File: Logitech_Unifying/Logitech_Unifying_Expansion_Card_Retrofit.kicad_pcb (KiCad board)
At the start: 2 copper layers, 24 x 27.3 mm, 9 parts, among them P1 USB_C_Plug_USB2.0, U1 AP2112K-3.3

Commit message: v1
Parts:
- removed C1, C2: 10uF, Capacitor_SMD:C_0805_2012Metric
- removed U1: AP2112K-3.3, Package_TO_SOT_SMD:SOT-23-5
- added DN: Castellated_2, Expansion_Card:Castellated_2, F.Cu at (138.9, 138.6)
- added DP: Castellated_2, Expansion_Card:Castellated_2, F.Cu at (141.1, 138.6)
- added GND: Logitech_Unifying_Reciever, Expansion_Card:Logitech_Unifying_Reciever_no_pads, F.Cu at (140.0, 152.0)
- added GND: Castellated_2, Expansion_Card:Castellated_2, F.Cu at (143.6, 138.6)
- added VBUS: Castellated_2, Expansion_Card:Castellated_2, F.Cu at (136.4, 138.6)
- moved R1 4.28 mm to (132.7, 132.3), turned to 90 degrees
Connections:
- P1 pad A6: (no net) -> /USB_DP
- P1 pad A7: (no net) -> /USB_DN
- P1 pad B5: (no net) -> unconnected-(P1-VCONN-PadB5)
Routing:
- net VBUS: track 0.00 -> 20.0 mm, vias 0 -> 2
- net /USB_DP: track 0.00 -> 9.74 mm, vias 0 -> 2
- net /USB_DN: track 0.00 -> 9.55 mm
- net Net-(P1-CC): track 0.00 -> 9.55 mm, vias 0 -> 2
- net GND: track 0.00 -> 6.21 mm, vias 8 -> 9
- added copper zone on B.Cu, net GND
- added copper zone on F.Cu, net GND
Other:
- outline, holes or cut-outs redrawn
- board text added: "5.1k"

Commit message: small revision for cadlab test
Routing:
- net GND: track 6.21 -> 5.86 mm, vias 9 -> 19
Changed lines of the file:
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@@
     (pad_to_mask_clearance 0)
     (pcbplotparams
-      (layerselection 0x0001000_7ffffffe)
+      (layerselection 0x00010fc_ffffffff)
       (plot_on_all_layers_selection 0x0000000_00000000)
       (disableapertmacros false)
@@
       (usegerberattributes true)
       (usegerberadvancedattributes true)
-      (creategerberjobfile true)
+      (creategerberjobfile false)
       (dashed_line_dash_ratio 12.000000)
       (dashed_line_gap_ratio 3.000000)
@@
       (sketchpadsonfab false)
       (subtractmaskfromsilk false)
-      (outputformat 3)
+      (outputformat 1)
       (mirror false)
       (drillshape 0)
       (scaleselection 1)
-      (outputdirectory "")
+      (outputdirectory "assembly/")
     )
   )
@@
     (property "ki_keywords" "r resistor")
     (attr smd)
-    (fp_text reference "R1" (at 0 -1.43) (layer "F.SilkS")
-        (effects (font (size 0.5842 0.5842) (thickness 0.1016)))
+    (fp_text reference "R1" (at 0.1 -1.55) (layer "F.SilkS")
+        (effects (font (size 0.8 0.8) (thickness 0.1016)))
     )
     (fp_text value "5.1k" (at 0 1.43 90) (layer "F.Fab")
@@
     (attr smd)
     (fp_text reference "P1" (at 0 2.04) (layer "F.SilkS")
-        (effects (font (size 0.5842 0.5842) (thickness 0.1016)))
+        (effects (font (size 0.8 0.8) (thickness 0.1016)))
     )
     (fp_text value "USB_C_Plug_USB2.0" (at 0 -1.96) (layer "F.Fab")
@@
     (tags "Through hole pin header THT 1x01 2.54mm single row")
     (attr through_hole)
-    (fp_text reference "VBUS" (at 0 -2.33) (layer "F.SilkS")
+    (fp_text reference "VBUS" (at -1.3 -2.35) (layer "F.SilkS")
         (effects (font (size 1 1) (thickness 0.15)))
     )
@@
     (tags "Through hole pin header THT 1x01 2.54mm single row")
     (attr through_hole)
-    (fp_text reference "DN" (at 0 -2.33) (layer "F.SilkS")
+    (fp_text reference "DN" (at -0.2 -2.3) (layer "F.SilkS")
         (effects (font (size 1 1) (thickness 0.15)))
     )
@@
     (tags "Through hole pin header THT 1x01 2.54mm single row")
     (attr through_hole)
-    (fp_text reference "GND" (at 0 -2.33) (layer "F.SilkS")
+    (fp_text reference "GND" (at 0.45 -2.3) (layer "F.SilkS")
         (effects (font (size 1 1) (thickness 0.15)))
     )
@@
   (gr_circle (center 128.7 146.5) (end 131.15 146.5)
     (stroke (width 0.05) (type solid)) (fill none) (layer "F.CrtYd"))
-  (gr_text "5.1k" (at 130.85 133.15) (layer "F.SilkS")
-    (effects (font (size 0.5842 0.5842) (thickness 0.1016)))
+  (gr_text "5.1k" (at 130.6 133.35) (layer "F.SilkS")
+    (effects (font (size 0.8 0.8) (thickness 0.1016)))
   )
   (segment (start 137.232999 129.22) (end 136.562999 129.89) (width 0.1524) (layer "F.Cu") (net 1))
   (segment (start 142.75 131.05) (end 142.75 129.067001) (width 0.1524) (layer "F.Cu") (net 1))
+  (via (at 128.8 145) (size 0.5) (drill 0.3) (layers "F.Cu" "B.Cu") (net 1))
+  (via (at 128.85 148.05) (size 0.5) (drill 0.3) (layers "F.Cu" "B.Cu") (net 1))
   (via (at 133.985 127.8255) (size 0.5) (drill 0.3) (layers "F.Cu" "B.Cu") (net 1))
+  (via (at 151.25 148.05) (size 0.5) (drill 0.3) (layers "F.Cu" "B.Cu") (net 1))
+  (via (at 129.9 147.55) (size 0.5) (drill 0.3) (layers "F.Cu" "B.Cu") (net 1))
   (via (at 137.9 135) (size 0.5) (drill 0.3) (layers "F.Cu" "B.Cu") (net 1))
   (via (at 133.985 128.778) (size 0.5) (drill 0.3) (layers "F.Cu" "B.Cu") (net 1))
+  (via (at 130.3 146.5) (size 0.5) (drill 0.3) (layers "F.Cu" "B.Cu") (net 1))
+  (via (at 129.85 145.45) (size 0.5) (drill 0.3) (layers "F.Cu" "B.Cu") (net 1))
+  (via (at 151.3 145) (size 0.5) (drill 0.3) (layers "F.Cu" "B.Cu") (net 1))
+  (via (at 149.8 146.5) (size 0.5) (drill 0.3) (layers "F.Cu" "B.Cu") (net 1))
   (via (at 134.9375 127.8255) (size 0.5) (drill 0.3) (layers "F.Cu" "B.Cu") (net 1))
+  (via (at 150.25 145.45) (size 0.5) (drill 0.3) (layers "F.Cu" "B.Cu") (net 1))
   (via (at 145.0975 127.8255) (size 0.5) (drill 0.3) (layers "F.Cu" "B.Cu") (net 1))
+  (via (at 150.2 147.55) (size 0.5) (drill 0.3) (layers "F.Cu" "B.Cu") (net 1))
   (via (at 145.0975 128.778) (size 0.5) (drill 0.3) (layers "F.Cu" "B.Cu") (net 1))
   (via (at 134.9375 128.778) (size 0.5) (drill 0.3) (layers "F.Cu" "B.Cu") (net 1))
@@
   (via (at 145.9865 128.778) (size 0.5) (drill 0.3) (layers "F.Cu" "B.Cu") (net 1))
   (segment (start 143.42 129.88) (end 142.75 129.21) (width 0.1524) (layer "B.Cu") (net 1))
-  (segment (start 142.75 129.21) (end 142.75 128.8585) (width 0.1524) (layer "B.Cu") (net 1))
   (segment (start 137.25 130.991499) (end 137.25 129.0085) (width 0.1524) (layer "B.Cu") (net 1))
   (segment (start 136.25 131.8) (end 134.925 133.125) (width 0.1524) (layer "F.Cu") (net 2))
   (segment (start 139.259204 129.076205) (end 139.259204 131.190796) (width 0.1524) (layer "F.Cu") (net 2))
-  (segment (start 138.65 131.8) (end 138.7 131.75) (width 0.1524) (layer "F.Cu") (net 2))
   (segment (start 139.259204 131.190796) (end 138.65 131.8) (width 0.1524) (layer "F.Cu") (net 2))
   (segment (start 134.925 133.125) (end 132.7 133.125) (width 0.1524) (layer "F.Cu") (net 2))
@@
   (segment (start 139.732999 129.05) (end 139.732999 129.800001) (width 0.2) (layer "F.Cu") (net 4))
   (segment (start 139.757999 131.691501) (end 139.757999 129.825001) (width 0.2) (layer "F.Cu") (net 4))
-  (segment (start 141.1 138.026014) (end 141.001254 138.12476) (width 0.2) (layer "F.Cu") (net 4))
   (via (at 139.65 131.7995) (size 0.5) (drill 0.3) (layers "F.Cu" "B.Cu") (net 4))
   (via (at 141.1 134) (size 0.5) (drill 0.3) (layers "F.Cu" "B.Cu") (net 4))
@@
         (xy 152.3 154.9)
         (xy 127.05 154.95)
-        (xy 126.95 126.25)
-        (xy 126.95 126.25)
       )
     )

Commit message: small change to test cadlab
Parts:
- moved R1 1.16 mm to (133.8, 131.8), turned to 180 degrees
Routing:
- net Net-(P1-CC): track 9.47 -> 7.05 mm
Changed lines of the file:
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@@
   (net 6 "unconnected-(P1-VCONN-PadB5)")
   (footprint "Resistor_SMD:R_0603_1608Metric" (layer "F.Cu")
-    (at 132.7 132.3 90)
+    (at 133.75 131.8 180)
     (descr "Resistor SMD 0603 (1608 Metric), square (rectangular) end terminal, IPC_7351 nominal, (Body size source: IPC-SM-782 page 72, https://www.pcb-3d.com/wordpress/wp-content/uploads/ipc-sm-782a_amendment_1_and_2.pdf), generated with kicad-footprint-generator")
     (tags "resistor")
@@
     (property "ki_keywords" "r resistor")
     (attr smd)
-    (fp_text reference "R1" (at 0.1 -1.55) (layer "F.SilkS")
+    (fp_text reference "R1" (at 0.1 -1.55 90) (layer "F.SilkS")
         (effects (font (size 0.8 0.8) (thickness 0.1016)))
     )
-    (fp_text value "5.1k" (at 0 1.43 90) (layer "F.Fab")
+    (fp_text value "5.1k" (at 0 1.43) (layer "F.Fab")
         (effects (font (size 1 1) (thickness 0.15)))
     )
-    (fp_text user "${REFERENCE}" (at 0 0 90) (layer "F.Fab")
+    (fp_text user "${REFERENCE}" (at 0 0) (layer "F.Fab")
         (effects (font (size 1 1) (thickness 0.15)))
     )
@@
     (fp_line (start 0.8 0.4125) (end -0.8 0.4125)
       (stroke (width 0.1) (type solid)) (layer "F.Fab"))
-    (pad "1" smd roundrect (at -0.825 0 90) (size 0.8 0.95) (layers "F.Cu" "F.Paste" "F.Mask") (roundrect_rratio 0.25)
+    (pad "1" smd roundrect (at -0.825 0 180) (size 0.8 0.95) (layers "F.Cu" "F.Paste" "F.Mask") (roundrect_rratio 0.25)
       (net 2 "Net-(P1-CC)") (pintype "passive"))
-    (pad "2" smd roundrect (at 0.825 0 90) (size 0.8 0.95) (layers "F.Cu" "F.Paste" "F.Mask") (roundrect_rratio 0.25)
+    (pad "2" smd roundrect (at 0.825 0 180) (size 0.8 0.95) (layers "F.Cu" "F.Paste" "F.Mask") (roundrect_rratio 0.25)
       (net 1 "GND") (pintype "passive"))
     (model "${KICAD6_3DMODEL_DIR}/Resistor_SMD.3dshapes/R_0603_1608Metric.wrl"
@@
   (gr_circle (center 128.7 146.5) (end 131.15 146.5)
     (stroke (width 0.05) (type solid)) (fill none) (layer "F.CrtYd"))
-  (gr_text "5.1k" (at 130.6 133.35) (layer "F.SilkS")
+  (gr_text "5.1k" (at 132.5 134.05 90) (layer "F.SilkS")
     (effects (font (size 0.8 0.8) (thickness 0.1016)))
   )
@@
   (segment (start 143.42 129.88) (end 142.75 129.21) (width 0.1524) (layer "B.Cu") (net 1))
   (segment (start 137.25 130.991499) (end 137.25 129.0085) (width 0.1524) (layer "B.Cu") (net 1))
-  (segment (start 136.25 131.8) (end 134.925 133.125) (width 0.1524) (layer "F.Cu") (net 2))
+  (segment (start 136.25 131.8) (end 134.575 131.8) (width 0.1524) (layer "F.Cu") (net 2))
   (segment (start 139.259204 129.076205) (end 139.259204 131.190796) (width 0.1524) (layer "F.Cu") (net 2))
   (segment (start 139.259204 131.190796) (end 138.65 131.8) (width 0.1524) (layer "F.Cu") (net 2))
-  (segment (start 134.925 133.125) (end 132.7 133.125) (width 0.1524) (layer "F.Cu") (net 2))
   (via (at 138.65 131.8) (size 0.5) (drill 0.3) (layers "F.Cu" "B.Cu") (net 2))
   (via (at 136.25 131.8) (size 0.5) (drill 0.3) (layers "F.Cu" "B.Cu") (net 2))

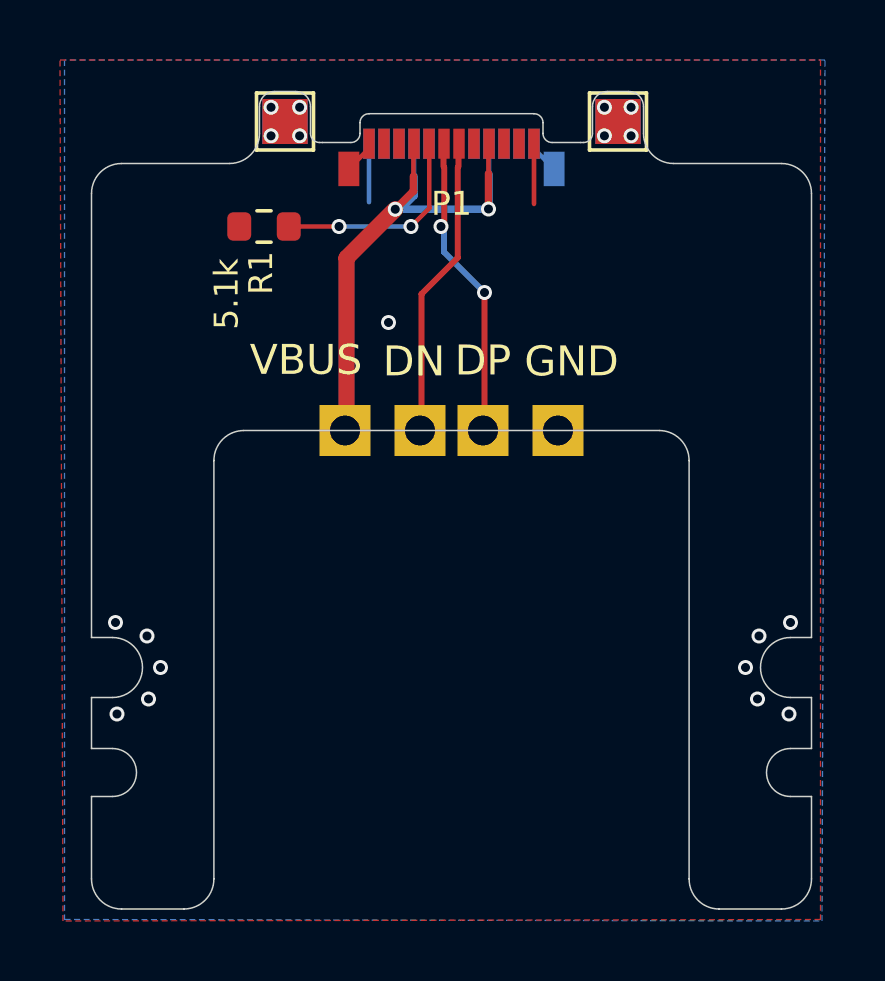
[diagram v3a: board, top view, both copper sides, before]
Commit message: flipped USB-C relative to reciever
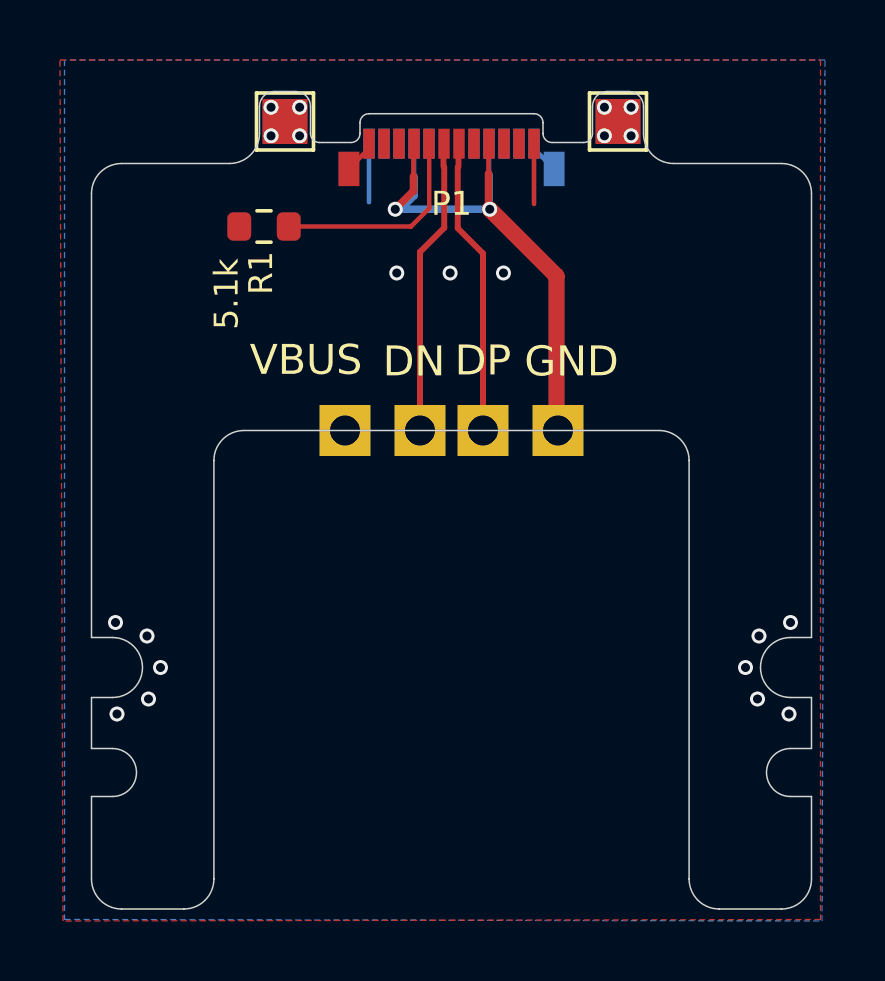
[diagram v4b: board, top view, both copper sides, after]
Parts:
- removed the GND at (140.0, 152.0)
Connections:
- DN pad 1: /USB_DN -> /USB_DP
- DP pad 1: /USB_DP -> /USB_DN
- GND pad 1: GND -> VBUS
- VBUS pad 1: VBUS -> GND
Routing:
- net VBUS: track 20.0 -> 20.8 mm
- net /USB_DP: track 9.60 -> 9.86 mm, vias 2 -> 0
- net Net-(P1-CC): vias 2 -> 0
- net GND: vias 19 -> 21

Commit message: increase USB-C mask bridge width for manufacture
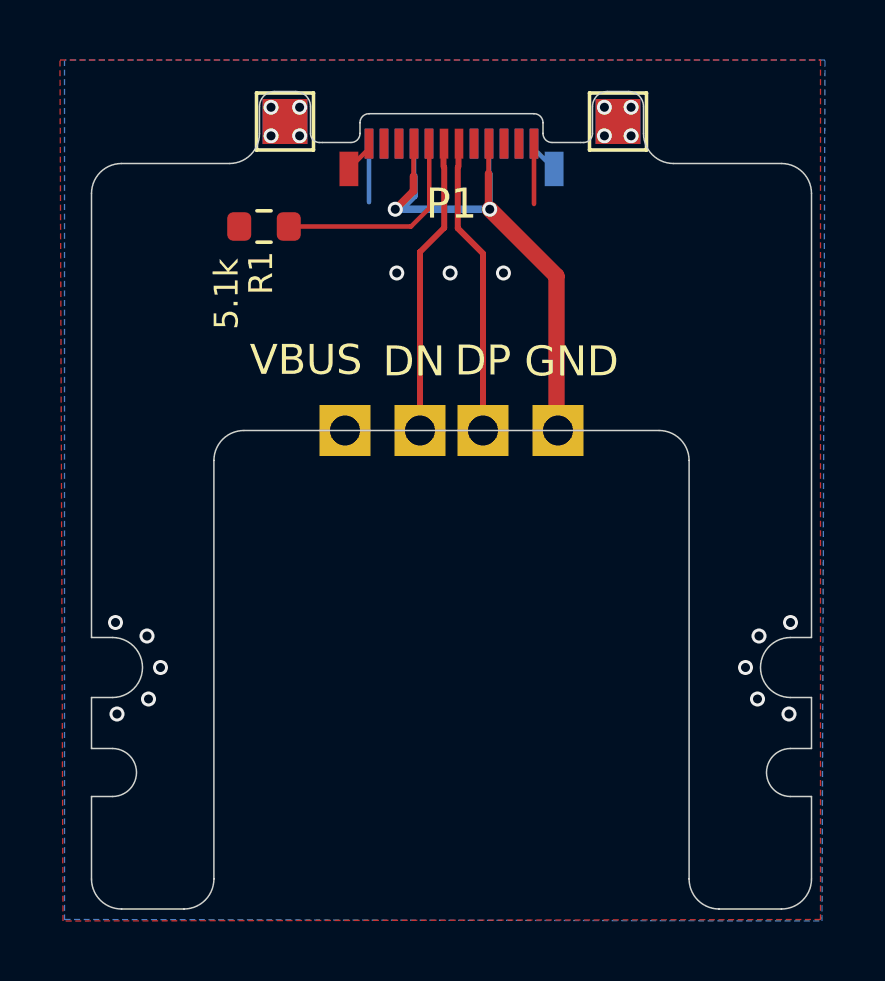
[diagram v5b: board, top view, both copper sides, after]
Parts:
- P1: footprint Expansion_Card:USB_C_Plug_Molex_105444 -> Expansion_Card:USB_C_Plug_Molex_105444_0.2mm_Spacing
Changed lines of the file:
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@@
     )
   )
-  (footprint "Expansion_Card:USB_C_Plug_Molex_105444" (layer "F.Cu")
+  (footprint "Expansion_Card:USB_C_Plug_Molex_105444_0.2mm_Spacing" (layer "F.Cu")
     (at 140 129)
     (descr "Universal Serial Bus (USB) Shielded I/O Plug, Type C, Right Angle, Surface Mount, http://www.molex.com/pdm_docs/sd/1054440001_sd.pdf")
@@
     (attr smd)
     (fp_text reference "P1" (at 0 2.04) (layer "F.SilkS")
-        (effects (font (size 0.8 0.8) (thickness 0.1016)))
+        (effects (font (size 1 1) (thickness 0.15)))
     )
     (fp_text value "USB_C_Plug_USB2.0" (at 0 -1.96) (layer "F.Fab")
@@
     )
     (fp_text user "${REFERENCE}" (at 0 2.04) (layer "F.Fab")
-        (effects (font (size 1 1) (thickness 0.15)))
+        (effects (font (size 1 1) (thickness 0.1)))
     )
     (fp_line (start -3.35 0) (end -4.3 0)
@@
     (fp_line (start 4.3 1.96) (end 4.3 -1.46)
       (stroke (width 0.05) (type solid)) (layer "F.CrtYd"))
-    (pad "A1" smd rect (at -2.75 0.04) (size 0.38 1) (layers "F.Cu" "F.Paste" "F.Mask")
+    (pad "A1" smd rect (at -2.75 0.04) (size 0.29 1) (layers "F.Cu" "F.Paste" "F.Mask")
       (net 1 "GND") (pinfunction "GND") (pintype "passive"))
-    (pad "A2" smd rect (at -2.25 0.04) (size 0.38 1) (layers "F.Cu" "F.Paste" "F.Mask"))
-    (pad "A3" smd rect (at -1.75 0.04) (size 0.38 1) (layers "F.Cu" "F.Paste" "F.Mask"))
-    (pad "A4" smd rect (at -1.25 0.04) (size 0.38 1) (layers "F.Cu" "F.Paste" "F.Mask")
+    (pad "A2" smd rect (at -2.25 0.04) (size 0.29 1) (layers "F.Cu" "F.Paste" "F.Mask"))
+    (pad "A3" smd rect (at -1.75 0.04) (size 0.29 1) (layers "F.Cu" "F.Paste" "F.Mask"))
+    (pad "A4" smd rect (at -1.25 0.04) (size 0.29 1) (layers "F.Cu" "F.Paste" "F.Mask")
       (net 3 "VBUS") (pinfunction "VBUS") (pintype "passive"))
-    (pad "A5" smd rect (at -0.75 0.04) (size 0.38 1) (layers "F.Cu" "F.Paste" "F.Mask")
+    (pad "A5" smd rect (at -0.75 0.04) (size 0.29 1) (layers "F.Cu" "F.Paste" "F.Mask")
       (net 2 "Net-(P1-CC)") (pinfunction "CC") (pintype "bidirectional"))
-    (pad "A6" smd rect (at -0.25 0.04) (size 0.38 1) (layers "F.Cu" "F.Paste" "F.Mask")
+    (pad "A6" smd rect (at -0.25 0.04) (size 0.29 1) (layers "F.Cu" "F.Paste" "F.Mask")
       (net 4 "/USB_DP") (pinfunction "D+") (pintype "bidirectional"))
-    (pad "A7" smd rect (at 0.25 0.04) (size 0.38 1) (layers "F.Cu" "F.Paste" "F.Mask")
+    (pad "A7" smd rect (at 0.25 0.04) (size 0.29 1) (layers "F.Cu" "F.Paste" "F.Mask")
       (net 5 "/USB_DN") (pinfunction "D-") (pintype "bidirectional"))
-    (pad "A8" smd rect (at 0.75 0.04) (size 0.38 1) (layers "F.Cu" "F.Paste" "F.Mask"))
-    (pad "A9" smd rect (at 1.25 0.04) (size 0.38 1) (layers "F.Cu" "F.Paste" "F.Mask")
+    (pad "A8" smd rect (at 0.75 0.04) (size 0.29 1) (layers "F.Cu" "F.Paste" "F.Mask"))
+    (pad "A9" smd rect (at 1.25 0.04) (size 0.29 1) (layers "F.Cu" "F.Paste" "F.Mask")
       (net 3 "VBUS") (pinfunction "VBUS") (pintype "passive"))
-    (pad "A10" smd rect (at 1.75 0.04) (size 0.38 1) (layers "F.Cu" "F.Paste" "F.Mask"))
-    (pad "A11" smd rect (at 2.25 0.04) (size 0.38 1) (layers "F.Cu" "F.Paste" "F.Mask"))
-    (pad "A12" smd rect (at 2.75 0.04) (size 0.38 1) (layers "F.Cu" "F.Paste" "F.Mask")
+    (pad "A10" smd rect (at 1.75 0.04) (size 0.29 1) (layers "F.Cu" "F.Paste" "F.Mask"))
+    (pad "A11" smd rect (at 2.25 0.04) (size 0.29 1) (layers "F.Cu" "F.Paste" "F.Mask"))
+    (pad "A12" smd rect (at 2.75 0.04) (size 0.29 1) (layers "F.Cu" "F.Paste" "F.Mask")
       (net 1 "GND") (pinfunction "GND") (pintype "passive"))
-    (pad "B1" smd rect (at 2.75 0.04) (size 0.38 1) (layers "B.Cu" "B.Paste" "B.Mask")
+    (pad "B1" smd rect (at 2.75 0.04) (size 0.29 1) (layers "B.Cu" "B.Paste" "B.Mask")
       (net 1 "GND") (pinfunction "GND") (pintype "passive"))
-    (pad "B2" smd rect (at 2.25 0.04) (size 0.38 1) (layers "B.Cu" "B.Paste" "B.Mask"))
-    (pad "B3" smd rect (at 1.75 0.04) (size 0.38 1) (layers "B.Cu" "B.Paste" "B.Mask"))
-    (pad "B4" smd rect (at 1.25 0.04) (size 0.38 1) (layers "B.Cu" "B.Paste" "B.Mask")
+    (pad "B2" smd rect (at 2.25 0.04) (size 0.29 1) (layers "B.Cu" "B.Paste" "B.Mask"))
+    (pad "B3" smd rect (at 1.75 0.04) (size 0.29 1) (layers "B.Cu" "B.Paste" "B.Mask"))
+    (pad "B4" smd rect (at 1.25 0.04) (size 0.29 1) (layers "B.Cu" "B.Paste" "B.Mask")
       (net 3 "VBUS") (pinfunction "VBUS") (pintype "passive"))
-    (pad "B5" smd rect (at 0.75 0.04) (size 0.38 1) (layers "B.Cu" "B.Paste" "B.Mask")
+    (pad "B5" smd rect (at 0.75 0.04) (size 0.29 1) (layers "B.Cu" "B.Paste" "B.Mask")
       (net 6 "unconnected-(P1-VCONN-PadB5)") (pinfunction "VCONN") (pintype "bidirectional+no_connect"))
-    (pad "B8" smd rect (at -0.75 0.04) (size 0.38 1) (layers "B.Cu" "B.Paste" "B.Mask"))
-    (pad "B9" smd rect (at -1.25 0.04) (size 0.38 1) (layers "B.Cu" "B.Paste" "B.Mask")
+    (pad "B8" smd rect (at -0.75 0.04) (size 0.29 1) (layers "B.Cu" "B.Paste" "B.Mask"))
+    (pad "B9" smd rect (at -1.25 0.04) (size 0.29 1) (layers "B.Cu" "B.Paste" "B.Mask")
       (net 3 "VBUS") (pinfunction "VBUS") (pintype "passive"))
-    (pad "B10" smd rect (at -1.75 0.04) (size 0.38 1) (layers "B.Cu" "B.Paste" "B.Mask"))
-    (pad "B11" smd rect (at -2.25 0.04) (size 0.38 1) (layers "B.Cu" "B.Paste" "B.Mask"))
-    (pad "B12" smd rect (at -2.75 0.04) (size 0.38 1) (layers "B.Cu" "B.Paste" "B.Mask")
+    (pad "B10" smd rect (at -1.75 0.04) (size 0.29 1) (layers "B.Cu" "B.Paste" "B.Mask"))
+    (pad "B11" smd rect (at -2.25 0.04) (size 0.29 1) (layers "B.Cu" "B.Paste" "B.Mask"))
+    (pad "B12" smd rect (at -2.75 0.04) (size 0.29 1) (layers "B.Cu" "B.Paste" "B.Mask")
       (net 1 "GND") (pinfunction "GND") (pintype "passive"))
-    (pad "S1" smd rect (at -3.42 0.88) (size 0.7 1.15) (layers "F.Cu" "F.Paste" "F.Mask")
+    (pad "S1" smd rect (at -3.42 0.88) (size 0.63 1.15) (layers "F.Cu" "F.Paste" "F.Mask")
       (net 1 "GND") (pinfunction "SHIELD") (pintype "passive"))
-    (pad "S1" smd rect (at 3.42 0.88) (size 0.7 1.15) (layers "B.Cu" "B.Paste" "B.Mask")
+    (pad "S1" smd rect (at 3.42 0.88) (size 0.63 1.15) (layers "B.Cu" "B.Paste" "B.Mask")
       (net 1 "GND") (pinfunction "SHIELD") (pintype "passive"))
     (model "${KISYS3DMOD}/Connector_USB.3dshapes/USB_C_Plug_Molex_105444.wrl"
